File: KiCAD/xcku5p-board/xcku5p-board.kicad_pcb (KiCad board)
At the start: 2 copper layers, 191 x 125.5 mm, 35 parts, among them U1 ADV7513BSWZ

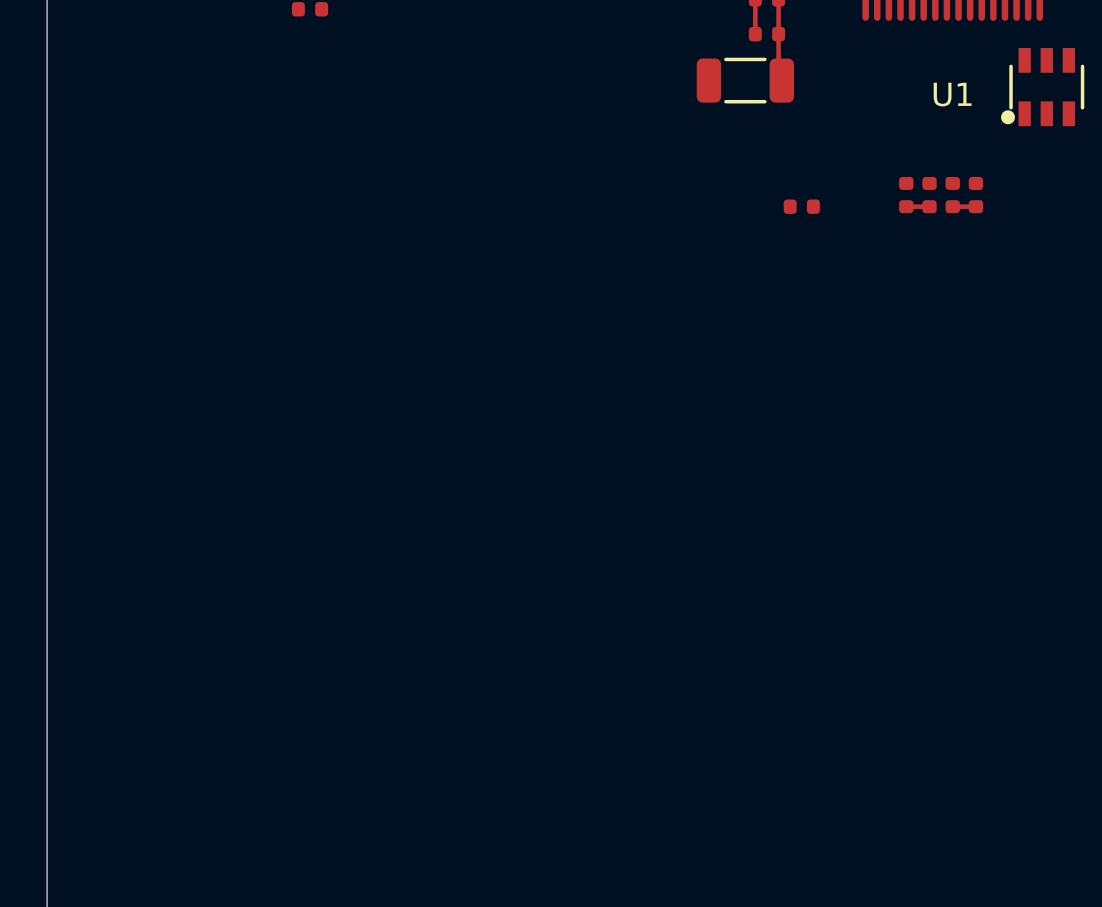
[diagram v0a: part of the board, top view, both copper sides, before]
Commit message: Add SD card circuit
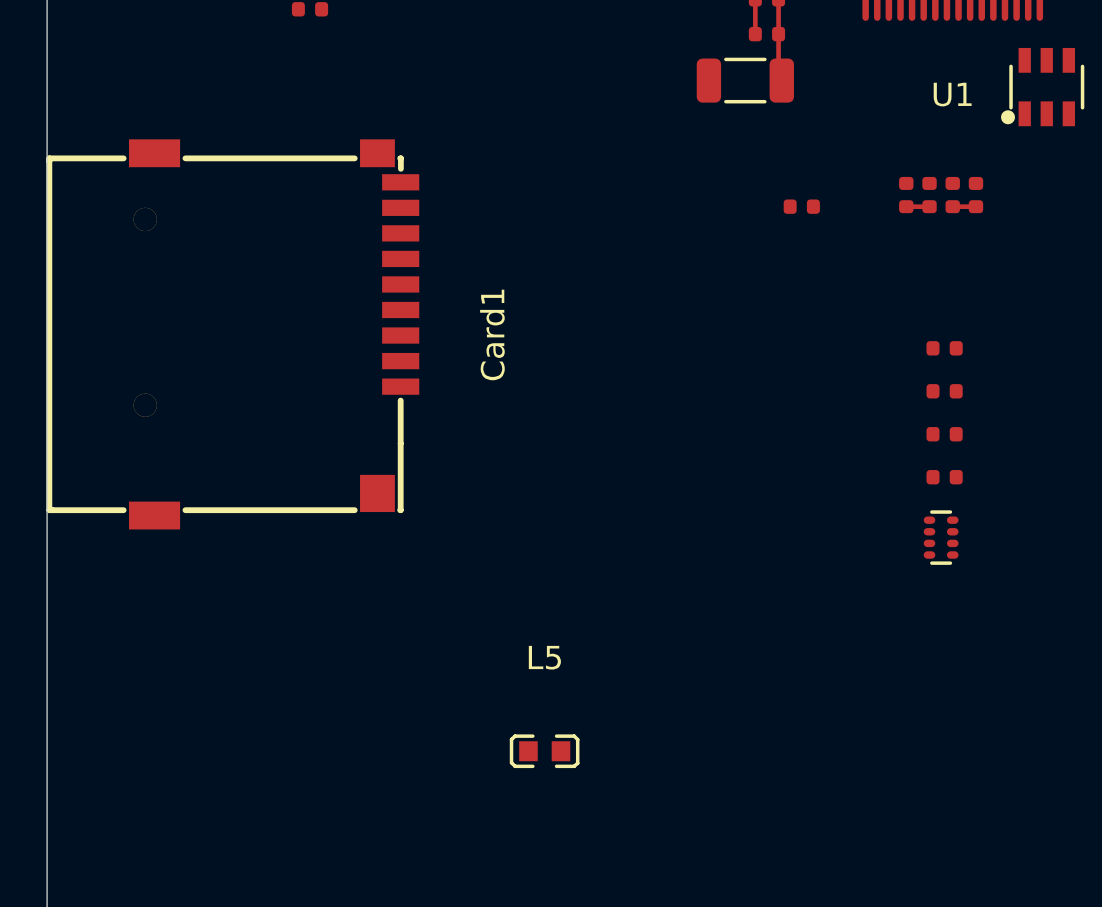
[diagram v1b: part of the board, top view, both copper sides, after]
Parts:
- added C16: 4.7uF, PCM_JLCPCB:C_0402, F.Cu at (72.7, 89.6)
- added C17: 100nF, PCM_JLCPCB:C_0402, F.Cu at (72.7, 91.5)
- added Card1: TF-012D, easyeda2kicad:TF-SMD_TF-012, F.Cu at (43.9, 89.0)
- added L5: CBW160808U300T, easyeda2kicad:L0603, F.Cu at (55.4, 107.0)
- added R12: 10kΩ, PCM_JLCPCB:R_0402x4, F.Cu at (72.5, 97.8)
- added R13: 10kΩ, PCM_JLCPCB:R_0402, F.Cu at (72.7, 93.3)
- added R14: 330kΩ, PCM_JLCPCB:R_0402, F.Cu at (72.7, 95.2)

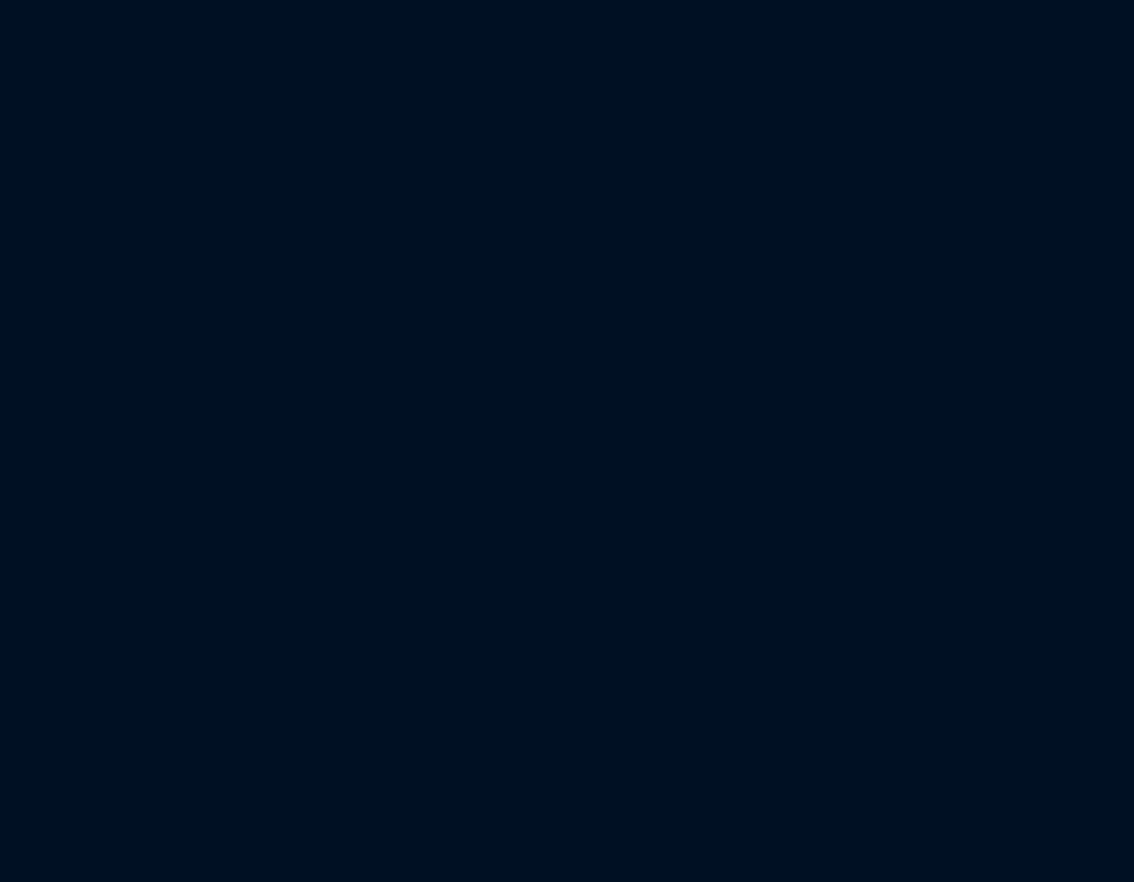
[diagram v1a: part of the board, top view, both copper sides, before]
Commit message: Add power circuit, switches, UART bridge
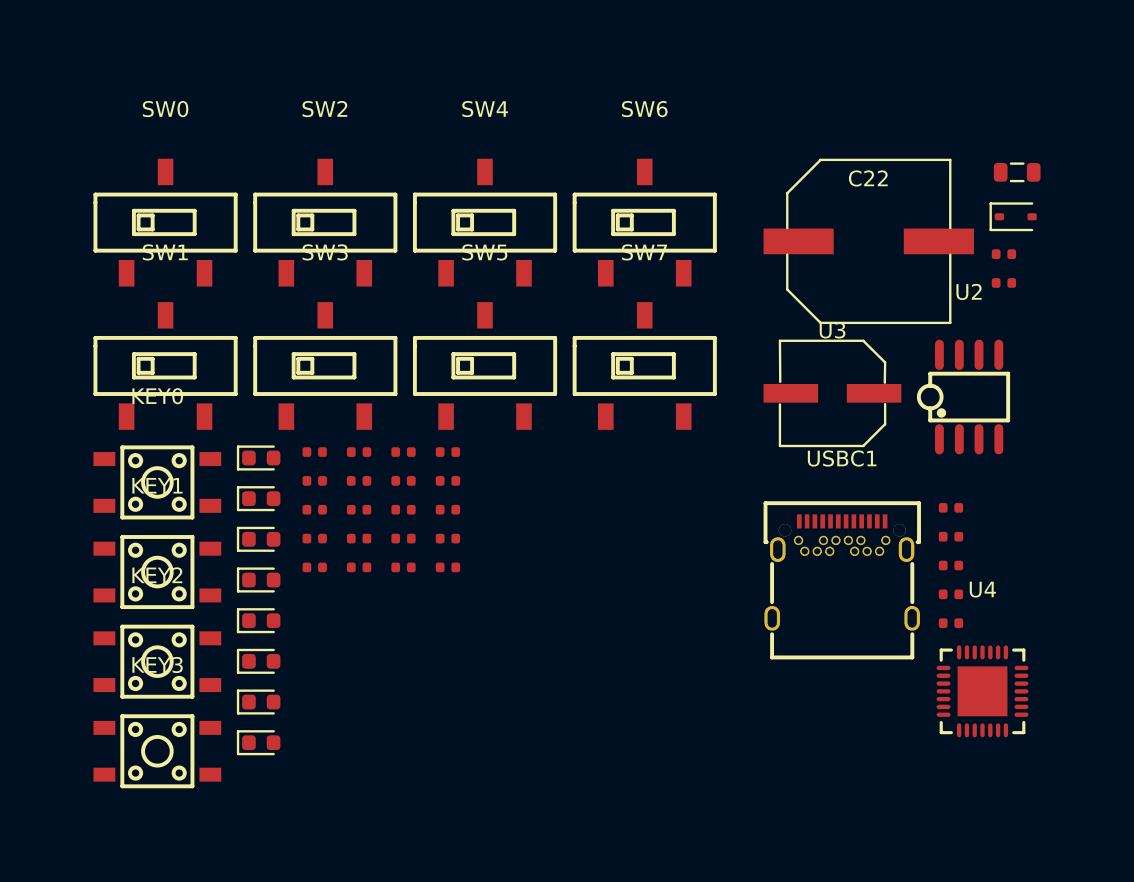
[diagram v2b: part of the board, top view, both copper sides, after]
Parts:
- added C18: 1uF, PCM_JLCPCB:C_0402, F.Cu at (207.5, 78.9)
- added C19: 100nF, PCM_JLCPCB:C_0402, F.Cu at (207.5, 80.8)
- added C20: 100nF, PCM_JLCPCB:C_0402, F.Cu at (207.5, 82.6)
- added C22: RVT1V471M1010 470UF 35V, easyeda2kicad:CAP-SMD_BD10.0-L10.3-W10.3-FD, F.Cu at (202.2, 61.8)
- added D4: 1N5819WS, PCM_JLCPCB:D_SOD-323, F.Cu at (211.7, 60.2)
- added KEY0: TS110916043, easyeda2kicad:SW-SMD_4P-L4.5-W4.5-P3.00-LS7.5, F.Cu at (156.6, 77.3)
- added KEY1: TS110916043, easyeda2kicad:SW-SMD_4P-L4.5-W4.5-P3.00-LS7.5, F.Cu at (156.6, 83.0)
- added KEY2: TS110916043, easyeda2kicad:SW-SMD_4P-L4.5-W4.5-P3.00-LS7.5, F.Cu at (156.6, 88.8)
- added KEY3: TS110916043, easyeda2kicad:SW-SMD_4P-L4.5-W4.5-P3.00-LS7.5, F.Cu at (156.6, 94.5)
- added L6: 22uH,5mA, PCM_JLCPCB:L_0805, F.Cu at (211.8, 57.4)
- added LED0: Red, PCM_JLCPCB:D_0603, F.Cu at (163.3, 75.7)
- added LED1: Red, PCM_JLCPCB:D_0603, F.Cu at (163.3, 78.3)
- added LED2: Red, PCM_JLCPCB:D_0603, F.Cu at (163.3, 80.9)
- added LED3: Red, PCM_JLCPCB:D_0603, F.Cu at (163.3, 83.5)
- added LED4: Red, PCM_JLCPCB:D_0603, F.Cu at (163.3, 86.1)
- added LED5: Red, PCM_JLCPCB:D_0603, F.Cu at (163.3, 88.8)
- added LED6: Red, PCM_JLCPCB:D_0603, F.Cu at (163.3, 91.4)
- added LED7: Red, PCM_JLCPCB:D_0603, F.Cu at (163.3, 94.0)
- added R15: 470Ω, PCM_JLCPCB:R_0402, F.Cu at (210.9, 62.6)
- added R16: 1kΩ, PCM_JLCPCB:R_0402, F.Cu at (210.9, 64.5)
- added R17: 10kΩ, PCM_JLCPCB:R_0402, F.Cu at (166.7, 75.3)
- added R18: 10kΩ, PCM_JLCPCB:R_0402, F.Cu at (166.7, 77.2)
- added R19: 10kΩ, PCM_JLCPCB:R_0402, F.Cu at (166.7, 79.0)
- added R20: 10kΩ, PCM_JLCPCB:R_0402, F.Cu at (166.7, 80.9)
- added R21: 10kΩ, PCM_JLCPCB:R_0402, F.Cu at (166.7, 82.7)
- added R22: 10kΩ, PCM_JLCPCB:R_0402, F.Cu at (169.5, 75.3)
- added R23: 10kΩ, PCM_JLCPCB:R_0402, F.Cu at (169.5, 77.2)
- added R24: 10kΩ, PCM_JLCPCB:R_0402, F.Cu at (169.5, 79.0)
- added R25: 10kΩ, PCM_JLCPCB:R_0402, F.Cu at (169.5, 80.9)
- added R26: 10kΩ, PCM_JLCPCB:R_0402, F.Cu at (169.5, 82.7)
- added R27: 10kΩ, PCM_JLCPCB:R_0402, F.Cu at (172.4, 75.3)
- added R28: 10kΩ, PCM_JLCPCB:R_0402, F.Cu at (172.4, 77.2)
- added R29: 330Ω, PCM_JLCPCB:R_0402, F.Cu at (172.4, 79.0)
- added R30: 330Ω, PCM_JLCPCB:R_0402, F.Cu at (172.4, 80.9)
- added R31: 330Ω, PCM_JLCPCB:R_0402, F.Cu at (172.4, 82.7)
- added R32: 330Ω, PCM_JLCPCB:R_0402, F.Cu at (175.2, 75.3)
- added R33: 330Ω, PCM_JLCPCB:R_0402, F.Cu at (175.2, 77.2)
- added R34: 330Ω, PCM_JLCPCB:R_0402, F.Cu at (175.2, 79.0)
- added R35: 330Ω, PCM_JLCPCB:R_0402, F.Cu at (175.2, 80.9)
- added R36: 330Ω, PCM_JLCPCB:R_0402, F.Cu at (175.2, 82.7)
- added R37: 5.1kΩ, PCM_JLCPCB:R_0402, F.Cu at (207.5, 84.5)
- added R38: 5.1kΩ, PCM_JLCPCB:R_0402, F.Cu at (207.5, 86.3)
- added SW0: K3-1235S, easyeda2kicad:SW-SMD_K3-1235S-K1, F.Cu at (157.1, 60.6)
- added SW1: K3-1235S, easyeda2kicad:SW-SMD_K3-1235S-K1, F.Cu at (157.1, 69.8)
- added SW2: K3-1235S, easyeda2kicad:SW-SMD_K3-1235S-K1, F.Cu at (167.4, 60.6)
- added SW3: K3-1235S, easyeda2kicad:SW-SMD_K3-1235S-K1, F.Cu at (167.4, 69.8)
- added SW4: K3-1235S, easyeda2kicad:SW-SMD_K3-1235S-K1, F.Cu at (177.6, 60.6)
- added SW5: K3-1235S, easyeda2kicad:SW-SMD_K3-1235S-K1, F.Cu at (177.6, 69.8)
- added SW6: K3-1235S, easyeda2kicad:SW-SMD_K3-1235S-K1, F.Cu at (187.9, 60.6)
- added SW7: K3-1235S, easyeda2kicad:SW-SMD_K3-1235S-K1, F.Cu at (187.9, 69.8)
- added U2: XL1509-ADJ, easyeda2kicad:SOIC-8_L5.0-W4.0-P1.27-LS6.0-BL, F.Cu at (208.7, 71.8)
- added U3: RVT0J331M0607_C2880037, easyeda2kicad:CAP-SMD_BD6.3-L6.6-W6.6-LS7.2-R-RD-1, F.Cu at (199.9, 71.6)
- added U4: CP2102-GMR, easyeda2kicad:WQFN-28_L5.0-W5.0-P0.50-BL-EP3.2, F.Cu at (209.6, 90.7)
- added USBC1: TYPE-C-31-M-04, easyeda2kicad:USB-C-SMD_TYPE-C-USB-20, F.Cu at (200.5, 82.9)
